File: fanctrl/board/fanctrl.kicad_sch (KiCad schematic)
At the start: 25 parts, among them J12 PROG, J2 Display, J5 Fan1, Q1 BXT420N03M, U3 ESP32-C3-WROOM-02, U3 FR8205, X1 12V

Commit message: fanctrl schema
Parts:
- removed Q1: BXT420N03M, Package_TO_SOT_SMD:SOT-23, symbol Transistor_FET:AO3400A
- added J3: Fan1, Drake:DG235-3.81-02P, symbol Connector_Generic:Conn_01x02
- added Q2: YJM04N10A, Package_TO_SOT_SMD:SOT-223, symbol Device:Q_NMOS_GDSD
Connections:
- net +12V: no longer J5.2 (Pin_2)
- net FAN_1: no longer R5.2, R6.1
- net GND: now also Q2.3 (S)
- net at D2.2 (A): now also Q2.2 (D), Q2.4 (D); no longer J5.1 (Pin_1)
- net at R6.2: now also Q2.1 (G)
- new net: R5.2, R6.1
- new net Driver/+12V: J5.2 (Pin_2)
- new net Driver/SW_GND: J5.1 (Pin_1)
- new net Driver1/+12V: J3.2 (Pin_2)
- new net Driver1/SW_GND: J3.1 (Pin_1)
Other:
- added sheet Driver (driver.kicad_sch)
- added sheet Driver1 (driver.kicad_sch)
- moved on the sheet: C7, D2, J5, R5, R6

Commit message: board design
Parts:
- removed D2: SK22, Diode_SMD:D_SMB_Handsoldering, symbol Device:D_Schottky
- removed J2: Display, Connector_PinHeader_2.54mm:PinHeader_1x03_P2.54mm_Vertical, symbol Connector_Generic:Conn_01x03
- removed Q2: YJM04N10A, Package_TO_SOT_SMD:SOT-223, symbol Device:Q_NMOS_GDSD
- removed R5: 10k, Resistor_SMD:R_0805_2012Metric_Pad1.20x1.40mm_HandSolder, symbol Device:R
- removed R6: 100, Resistor_SMD:R_0805_2012Metric_Pad1.20x1.40mm_HandSolder, symbol Device:R
- added J2: AUX, Connector_PinHeader_2.54mm:PinHeader_1x05_P2.54mm_Vertical, symbol Connector_Generic:Conn_01x05
- J3: value Fan1 -> Fan2
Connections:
- net +3V3: now also J2.5 (Pin_5)
- net GND: now also J2.1 (Pin_1)
- net AUX0: now reaches U3.11 (GPIO20/U0RXD)
- net AUX0: now also J2.2 (Pin_2)
- net AUX2: now reaches U3.16 (GPIO2/ADC1_CH2)
- net AUX2: now also J2.4 (Pin_4)
- net DISP renamed AUX1
- net AUX1: now also J2.3 (Pin_3)
- no-connect marks 9 -> 7

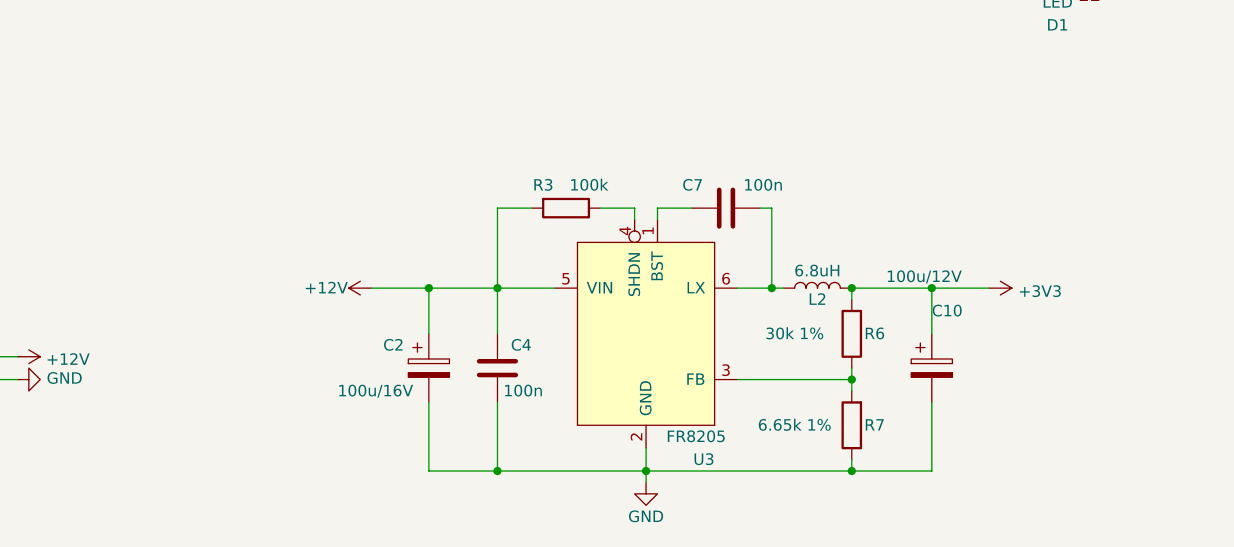
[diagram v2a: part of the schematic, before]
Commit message: ceramic capacitors on PSU & JLC order
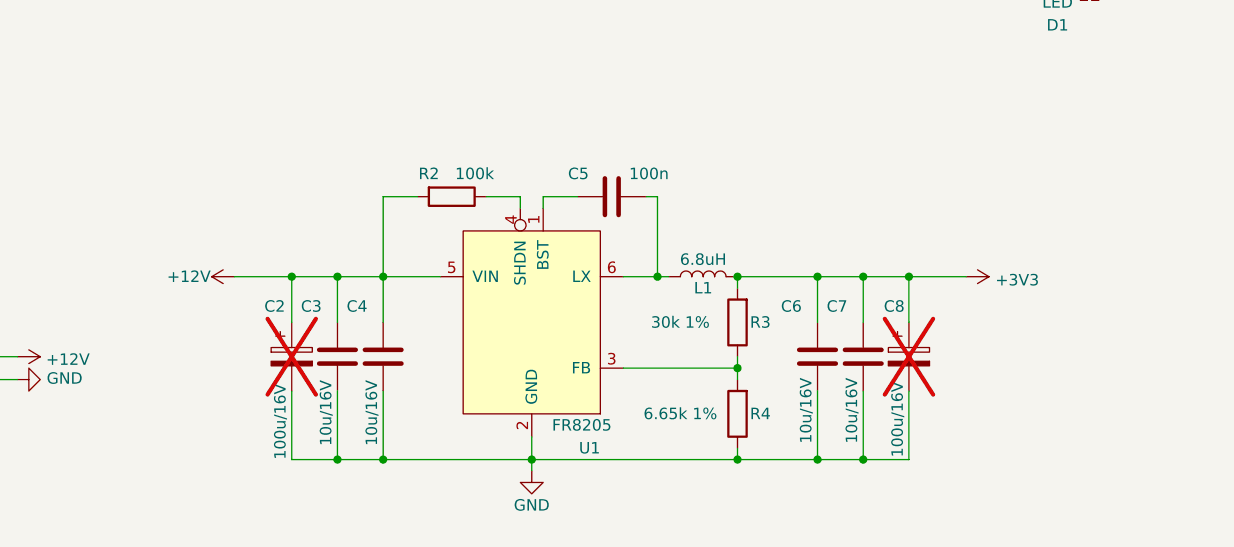
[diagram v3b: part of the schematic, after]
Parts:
- removed C10: 100u/12V, Capacitor_SMD:CP_Elec_6.3x5.4, symbol Device:C_Polarized
- removed L2: 6.8uH, Drake:CKCS6028, symbol Device:L
- removed R6: 30k 1%, Resistor_SMD:R_0805_2012Metric_Pad1.20x1.40mm_HandSolder, symbol Device:R
- removed R7: 6.65k 1%, Resistor_SMD:R_0805_2012Metric_Pad1.20x1.40mm_HandSolder, symbol Device:R
- removed U3: FR8205, Package_TO_SOT_SMD:SOT-23-6, symbol Drake:FR8205
- added C3, C6: 10u/16V, Capacitor_SMD:C_0805_2012Metric_Pad1.18x1.45mm_HandSolder, symbol Device:C
- added C5: 100n, Capacitor_SMD:C_0805_2012Metric_Pad1.18x1.45mm_HandSolder, symbol Device:C
- added C8: 100u/16V, Capacitor_SMD:CP_Elec_6.3x5.4, symbol Device:C_Polarized
- added L1: 6.8uH, Drake:CKCS6028, symbol Device:L
- added R2: 100k, Resistor_SMD:R_0805_2012Metric_Pad1.20x1.40mm_HandSolder, symbol Device:R
- added R4: 6.65k 1%, Resistor_SMD:R_0805_2012Metric_Pad1.20x1.40mm_HandSolder, symbol Device:R
- added U1: FR8205, Package_TO_SOT_SMD:SOT-23-6, symbol Drake:FR8205
- C2: now not fitted
- C4, C7: value 100n -> 10u/16V
- R3: value 100k -> 30k 1%
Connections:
- net +12V: now also C4.1, C3.1, R2.2, U1.5 (VIN); no longer C4.2, R3.2
- net +3V3: now also C7.1, R3.2, C6.1, C8.1, L1.2
- net GND: now also C4.2, C7.2, C3.2, C6.2, C8.2, R4.1, U1.2 (GND); no longer C4.1
- net at R3.1: now also R4.2, U1.3 (FB)
- new net: C5.1, U1.1 (BST)
- new net: R2.1, U1.4 (SHDN)
- new net: C5.2, L1.1, U1.6 (LX)
